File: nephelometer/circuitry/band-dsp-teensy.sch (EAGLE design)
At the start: 42 parts, among them IC1 LM4041CILP, IC2 AD822N, IC3 MCP6S21, J1 RJ11-6PTH, Q1 IRLB8721, T1 2N2222, T2 2N2222

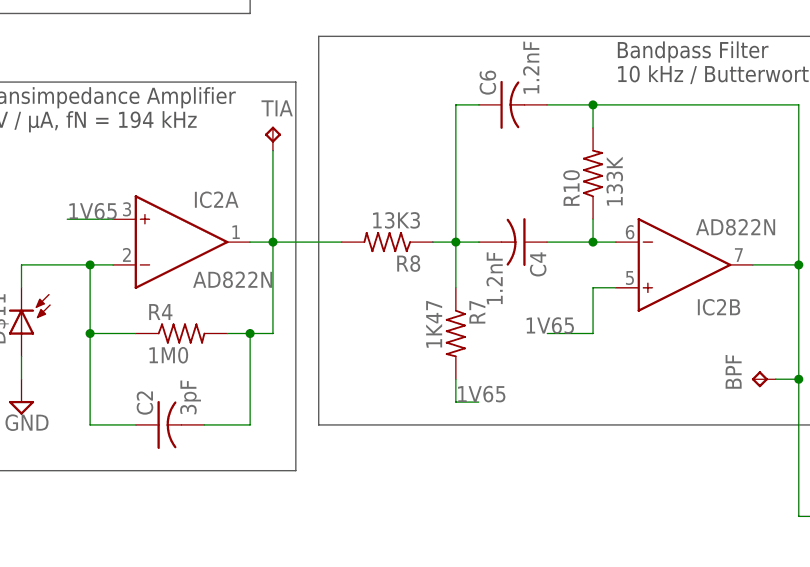
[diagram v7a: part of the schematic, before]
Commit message: Finalized parts and components for 10kHz band-pass etc
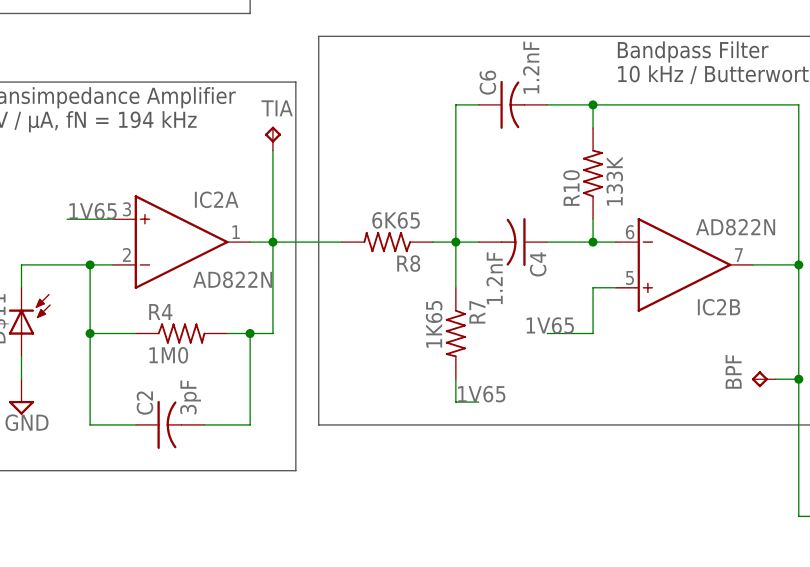
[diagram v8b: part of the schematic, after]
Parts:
- R7: value 1K47 -> 1K65; DIGIKEY# 1.50KXBK-ND -> 1.65KXBK-ND; MANF# MFR-25FBF52-1K5 -> MFR-25FBF52-1K65
- R8: value 13K3 -> 6K65; DIGIKEY# 13.3KXBK-ND -> 6.65KXBK-ND; MANF# MFR-25FBF52-13K3 -> MFR-25FBF52-6K65
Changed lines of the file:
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@@
 <attribute name="MANF#" value="K122J15C0GF5TL2"/>
 </part>
-<part name="R8" library="adafruit" deviceset="R-US_" device="0207/9" value="13K3">
-<attribute name="DIGIKEY#" value="13.3KXBK-ND"/>
+<part name="R8" library="adafruit" deviceset="R-US_" device="0207/9" value="6K65">
+<attribute name="DIGIKEY#" value="6.65KXBK-ND"/>
 <attribute name="MANF" value="Yageo"/>
-<attribute name="MANF#" value="MFR-25FBF52-13K3"/>
+<attribute name="MANF#" value="MFR-25FBF52-6K65"/>
 </part>
 <part name="R11" library="adafruit" deviceset="R-US_" device="0207/9" value="4K7">
@@
 <attribute name="MANF#" value="MFR-25FBF52-133K"/>
 </part>
-<part name="R7" library="adafruit" deviceset="R-US_" device="0207/9" value="1K47">
-<attribute name="DIGIKEY#" value="1.50KXBK-ND"/>
+<part name="R7" library="adafruit" deviceset="R-US_" device="0207/9" value="1K65">
+<attribute name="DIGIKEY#" value="1.65KXBK-ND"/>
 <attribute name="MANF" value="Yageo"/>
-<attribute name="MANF#" value="MFR-25FBF52-1K5"/>
+<attribute name="MANF#" value="MFR-25FBF52-1K65"/>
 </part>
 <part name="C8" library="adafruit" deviceset="C-US" device="025-030X050" value="10µF">
